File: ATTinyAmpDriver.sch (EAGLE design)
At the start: 28 parts, among them Q1 SI2301CDS, Q2 BC846, U1 SPX5205M5-L-3-3, U2 ATTINY5-TSHR, U3 MCP6L2-X_SN, X1 DIODES, X2 INPUT

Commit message: Working code and matching board and schematic
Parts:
- R3, R4: value 10k -> 3.9k
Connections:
- removed net INA+: C4.1, R4.2, U3.VINA+
- removed net VINB-: R8.1, R9.2, U3.VINB-
- new net INA-: R8.1, R9.2, U3.VINA-
- new net INB+: C4.1, R4.2, U3.VINB+
- net D-: now also U3.VINA+; no longer R3.1
- net MEASURE: now also C2.1, U3.VINB-; no longer R9.1
- net OUTA: now also R3.1, R9.1; no longer C2.1, U3.VINA-, U3.VINB+
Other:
- note added: "Q = .5 (ideal) f = 400Hz (~10% 3.77kHz PWM)"
- moved on the sheet: C4
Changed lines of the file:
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@@
 <attribute name="DIGIKEY_COST" value=".04"/>
 </part>
-<part name="R3" library="resistor" deviceset="R-US_" device="R0603" value="10k">
+<part name="R3" library="resistor" deviceset="R-US_" device="R0603" value="3.9k">
 <attribute name="DIGIKEY" value="RMCF0603FT10K0CT-ND"/>
 <attribute name="DIGIKEY_COST" value=".04"/>
@@
 <attribute name="DIGIKEY_COST" value=".64"/>
 </part>
-<part name="R4" library="resistor" deviceset="R-US_" device="R0603" value="10k">
+<part name="R4" library="resistor" deviceset="R-US_" device="R0603" value="3.9k">
 <attribute name="DIGIKEY" value="RMCF0603FT10K0CT-ND"/>
 <attribute name="DIGIKEY_COST" value=".04"/>
@@
 <wire x1="279.4" y1="215.9" x2="279.4" y2="0" width="0.1524" layer="98"/>
 <wire x1="279.4" y1="0" x2="0" y2="0" width="0.1524" layer="98"/>
-<text x="149.86" y="111.76" size="1.778" layer="91">Sallen Key PWM Input Filter</text>
+<text x="149.86" y="106.68" size="1.778" layer="91">Sallen Key PWM Input Filter</text>
+<text x="149.86" y="99.06" size="1.778" layer="91">Q = .5 (ideal)
+f = 400Hz (~10% 3.77kHz PWM)</text>
 </plain>
 <instances>
@@
 <attribute name="DIGIKEY_COST" x="165.1" y="124.46" size="1.778" layer="96" rot="MR180" display="off"/>
 </instance>
-<instance part="C4" gate="G$1" x="185.42" y="116.84">
-<attribute name="DIGIKEY" x="185.42" y="116.84" size="1.778" layer="96" display="off"/>
-<attribute name="DIGIKEY_COST" x="185.42" y="116.84" size="1.778" layer="96" display="off"/>
-</instance>
-<instance part="SUPPLY12" gate="GND" x="185.42" y="106.68"/>
+<instance part="C4" gate="G$1" x="190.5" y="116.84">
+<attribute name="DIGIKEY" x="190.5" y="116.84" size="1.778" layer="96" display="off"/>
+<attribute name="DIGIKEY_COST" x="190.5" y="116.84" size="1.778" layer="96" display="off"/>
+</instance>
+<instance part="SUPPLY12" gate="GND" x="190.5" y="106.68"/>
 <instance part="C6" gate="G$1" x="157.48" y="175.26">
 <attribute name="DIGIKEY" x="157.48" y="175.26" size="1.778" layer="96" display="off"/>
@@
 <pinref part="C4" gate="G$1" pin="2"/>
 <pinref part="SUPPLY12" gate="GND" pin="GND"/>
-<wire x1="185.42" y1="111.76" x2="185.42" y2="109.22" width="0.1524" layer="91"/>
-<wire x1="185.42" y1="109.22" x2="185.42" y2="106.68" width="0.1524" layer="91"/>
+<wire x1="190.5" y1="111.76" x2="190.5" y2="109.22" width="0.1524" layer="91"/>
+<wire x1="190.5" y1="109.22" x2="190.5" y2="106.68" width="0.1524" layer="91"/>
 </segment>
 <segment>
@@
 </segment>
 <segment>
-<pinref part="R3" gate="G$1" pin="1"/>
-<wire x1="160.02" y1="124.46" x2="157.48" y2="124.46" width="0.1524" layer="91"/>
-<label x="157.48" y="124.46" size="1.778" layer="95" rot="R180" xref="yes"/>
+<pinref part="U3" gate="A" pin="VINA+"/>
+<wire x1="193.04" y1="50.8" x2="190.5" y2="50.8" width="0.1524" layer="91"/>
+<label x="190.5" y="50.8" size="1.778" layer="95" rot="R180" xref="yes"/>
 </segment>
 </net>
@@
 </segment>
 <segment>
-<pinref part="R9" gate="G$1" pin="1"/>
-<wire x1="243.84" y1="132.08" x2="248.92" y2="132.08" width="0.1524" layer="91"/>
-<label x="248.92" y="132.08" size="1.778" layer="95" xref="yes"/>
-</segment>
-<segment>
 <pinref part="U3" gate="A" pin="VOUTB"/>
 <wire x1="233.68" y1="50.8" x2="241.3" y2="50.8" width="0.1524" layer="91"/>
 <label x="241.3" y="50.8" size="1.778" layer="95" xref="yes"/>
+</segment>
+<segment>
+<pinref part="C2" gate="G$1" pin="1"/>
+<wire x1="172.72" y1="137.16" x2="172.72" y2="142.24" width="0.1524" layer="91"/>
+<wire x1="172.72" y1="142.24" x2="162.56" y2="142.24" width="0.1524" layer="91"/>
+<label x="162.56" y="142.24" size="1.778" layer="95" rot="R180" xref="yes"/>
+</segment>
+<segment>
+<pinref part="U3" gate="A" pin="VINB-"/>
+<wire x1="193.04" y1="45.72" x2="182.88" y2="45.72" width="0.1524" layer="91"/>
+<label x="182.88" y="45.72" size="1.778" layer="95" rot="R180" xref="yes"/>
 </segment>
 </net>
@@
 </segment>
 </net>
-<net name="INA+" class="0">
-<segment>
-<pinref part="C4" gate="G$1" pin="1"/>
-<wire x1="185.42" y1="119.38" x2="185.42" y2="124.46" width="0.1524" layer="91"/>
-<pinref part="R4" gate="G$1" pin="2"/>
-<wire x1="185.42" y1="124.46" x2="193.04" y2="124.46" width="0.1524" layer="91"/>
-<label x="193.04" y="124.46" size="1.778" layer="95" xref="yes"/>
-</segment>
-<segment>
-<pinref part="U3" gate="A" pin="VINA+"/>
-<wire x1="193.04" y1="50.8" x2="180.34" y2="50.8" width="0.1524" layer="91"/>
-<label x="180.34" y="50.8" size="1.778" layer="95" rot="R180" xref="yes"/>
-</segment>
-</net>
 <net name="N$8" class="0">
 <segment>
@@
 </segment>
 <segment>
-<pinref part="U3" gate="A" pin="VINB+"/>
-<wire x1="193.04" y1="43.18" x2="180.34" y2="43.18" width="0.1524" layer="91"/>
-<label x="180.34" y="43.18" size="1.778" layer="95" rot="R180" xref="yes"/>
-</segment>
-<segment>
-<pinref part="C2" gate="G$1" pin="1"/>
-<wire x1="162.56" y1="142.24" x2="172.72" y2="142.24" width="0.1524" layer="91"/>
-<wire x1="172.72" y1="142.24" x2="172.72" y2="137.16" width="0.1524" layer="91"/>
-<label x="162.56" y="142.24" size="1.778" layer="95" rot="R180" xref="yes"/>
-</segment>
-<segment>
-<pinref part="U3" gate="A" pin="VINA-"/>
-<wire x1="193.04" y1="53.34" x2="190.5" y2="53.34" width="0.1524" layer="91"/>
-<label x="190.5" y="53.34" size="1.778" layer="95" rot="R180" xref="yes"/>
-</segment>
-</net>
-<net name="VINB-" class="0">
-<segment>
-<pinref part="U3" gate="A" pin="VINB-"/>
-<wire x1="193.04" y1="45.72" x2="190.5" y2="45.72" width="0.1524" layer="91"/>
-<label x="190.5" y="45.72" size="1.778" layer="95" rot="R180" xref="yes"/>
-</segment>
-<segment>
-<wire x1="220.98" y1="132.08" x2="228.6" y2="132.08" width="0.1524" layer="91"/>
-<pinref part="R9" gate="G$1" pin="2"/>
-<wire x1="228.6" y1="132.08" x2="228.6" y2="129.54" width="0.1524" layer="91"/>
-<wire x1="233.68" y1="132.08" x2="228.6" y2="132.08" width="0.1524" layer="91"/>
-<junction x="228.6" y="132.08"/>
-<label x="220.98" y="132.08" size="1.778" layer="95" rot="R180" xref="yes"/>
-<pinref part="R8" gate="G$1" pin="1"/>
+<pinref part="R9" gate="G$1" pin="1"/>
+<wire x1="243.84" y1="132.08" x2="251.46" y2="132.08" width="0.1524" layer="91"/>
+<label x="251.46" y="132.08" size="1.778" layer="95" xref="yes"/>
+</segment>
+<segment>
+<pinref part="R3" gate="G$1" pin="1"/>
+<wire x1="160.02" y1="124.46" x2="154.94" y2="124.46" width="0.1524" layer="91"/>
+<label x="154.94" y="124.46" size="1.778" layer="95" rot="R180" xref="yes"/>
 </segment>
 </net>
@@
 </segment>
 </net>
+<net name="INB+" class="0">
+<segment>
+<pinref part="R4" gate="G$1" pin="2"/>
+<pinref part="C4" gate="G$1" pin="1"/>
+<wire x1="185.42" y1="124.46" x2="190.5" y2="124.46" width="0.1524" layer="91"/>
+<wire x1="190.5" y1="124.46" x2="190.5" y2="119.38" width="0.1524" layer="91"/>
+<wire x1="190.5" y1="124.46" x2="195.58" y2="124.46" width="0.1524" layer="91"/>
+<junction x="190.5" y="124.46"/>
+<label x="195.58" y="124.46" size="1.778" layer="95" xref="yes"/>
+</segment>
+<segment>
+<pinref part="U3" gate="A" pin="VINB+"/>
+<wire x1="193.04" y1="43.18" x2="190.5" y2="43.18" width="0.1524" layer="91"/>
+<label x="190.5" y="43.18" size="1.778" layer="95" rot="R180" xref="yes"/>
+</segment>
+</net>
+<net name="INA-" class="0">
+<segment>
+<pinref part="U3" gate="A" pin="VINA-"/>
+<wire x1="193.04" y1="53.34" x2="182.88" y2="53.34" width="0.1524" layer="91"/>
+<label x="182.88" y="53.34" size="1.778" layer="95" rot="R180" xref="yes"/>
+</segment>
+<segment>
+<pinref part="R9" gate="G$1" pin="2"/>
+<wire x1="233.68" y1="132.08" x2="228.6" y2="132.08" width="0.1524" layer="91"/>
+<pinref part="R8" gate="G$1" pin="1"/>
+<wire x1="228.6" y1="132.08" x2="218.44" y2="132.08" width="0.1524" layer="91"/>
+<wire x1="228.6" y1="129.54" x2="228.6" y2="132.08" width="0.1524" layer="91"/>
+<junction x="228.6" y="132.08"/>
+<label x="218.44" y="132.08" size="1.778" layer="95" rot="R180" xref="yes"/>
+</segment>
+</net>

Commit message: Updated BOM
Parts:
- R3, R4: DIGIKEY RMCF0603FT10K0CT-ND -> RMCF0603FT3K90CT-ND
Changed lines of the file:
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@@
 </part>
 <part name="R3" library="resistor" deviceset="R-US_" device="R0603" value="3.9k">
-<attribute name="DIGIKEY" value="RMCF0603FT10K0CT-ND"/>
+<attribute name="DIGIKEY" value="RMCF0603FT3K90CT-ND"/>
 <attribute name="DIGIKEY_COST" value=".04"/>
 </part>
@@
 </part>
 <part name="R4" library="resistor" deviceset="R-US_" device="R0603" value="3.9k">
-<attribute name="DIGIKEY" value="RMCF0603FT10K0CT-ND"/>
+<attribute name="DIGIKEY" value="RMCF0603FT3K90CT-ND"/>
 <attribute name="DIGIKEY_COST" value=".04"/>
 </part>

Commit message: Added Newark pricing to some components
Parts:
- Q1: NEWARK (none) -> 16P3701; NEWARK_COST (none) -> .37
- Q2: NEWARK (none) -> 75R0728; NEWARK_COST (none) -> .14
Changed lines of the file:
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@@
 <attribute name="DIGIKEY" value="568-6956-1-ND"/>
 <attribute name="DIGIKEY_COST" value=".69"/>
+<attribute name="NEWARK" value="16P3701"/>
+<attribute name="NEWARK_COST" value=".37"/>
 </part>
 <part name="SUPPLY11" library="supply2" deviceset="+14V" device=""/>
@@
 <attribute name="DIGIKEY" value="BC846BMTFCT-ND"/>
 <attribute name="DIGIKEY_COST" value=".17"/>
+<attribute name="NEWARK" value="75R0728"/>
+<attribute name="NEWARK_COST" value=".14"/>
 </part>
 <part name="SUPPLY14" library="supply2" deviceset="GND" device=""/>
@@
 <attribute name="VALUE" x="90.17" y="66.04" size="1.778" layer="96" rot="MR180"/>
 <attribute name="NAME" x="92.71" y="76.2" size="1.778" layer="95" rot="MR180"/>
+<attribute name="NEWARK" x="96.52" y="71.12" size="1.778" layer="96" rot="MR180" display="off"/>
+<attribute name="NEWARK_COST" x="96.52" y="71.12" size="1.778" layer="96" rot="MR180" display="off"/>
 </instance>
 <instance part="SUPPLY11" gate="G$1" x="101.6" y="93.98"/>
@@
 <attribute name="DIGIKEY" x="76.2" y="60.96" size="1.778" layer="96" display="off"/>
 <attribute name="DIGIKEY_COST" x="76.2" y="60.96" size="1.778" layer="96" display="off"/>
+<attribute name="NEWARK" x="76.2" y="60.96" size="1.778" layer="96" display="off"/>
+<attribute name="NEWARK_COST" x="76.2" y="60.96" size="1.778" layer="96" display="off"/>
 </instance>
 <instance part="SUPPLY14" gate="GND" x="78.74" y="50.8"/>

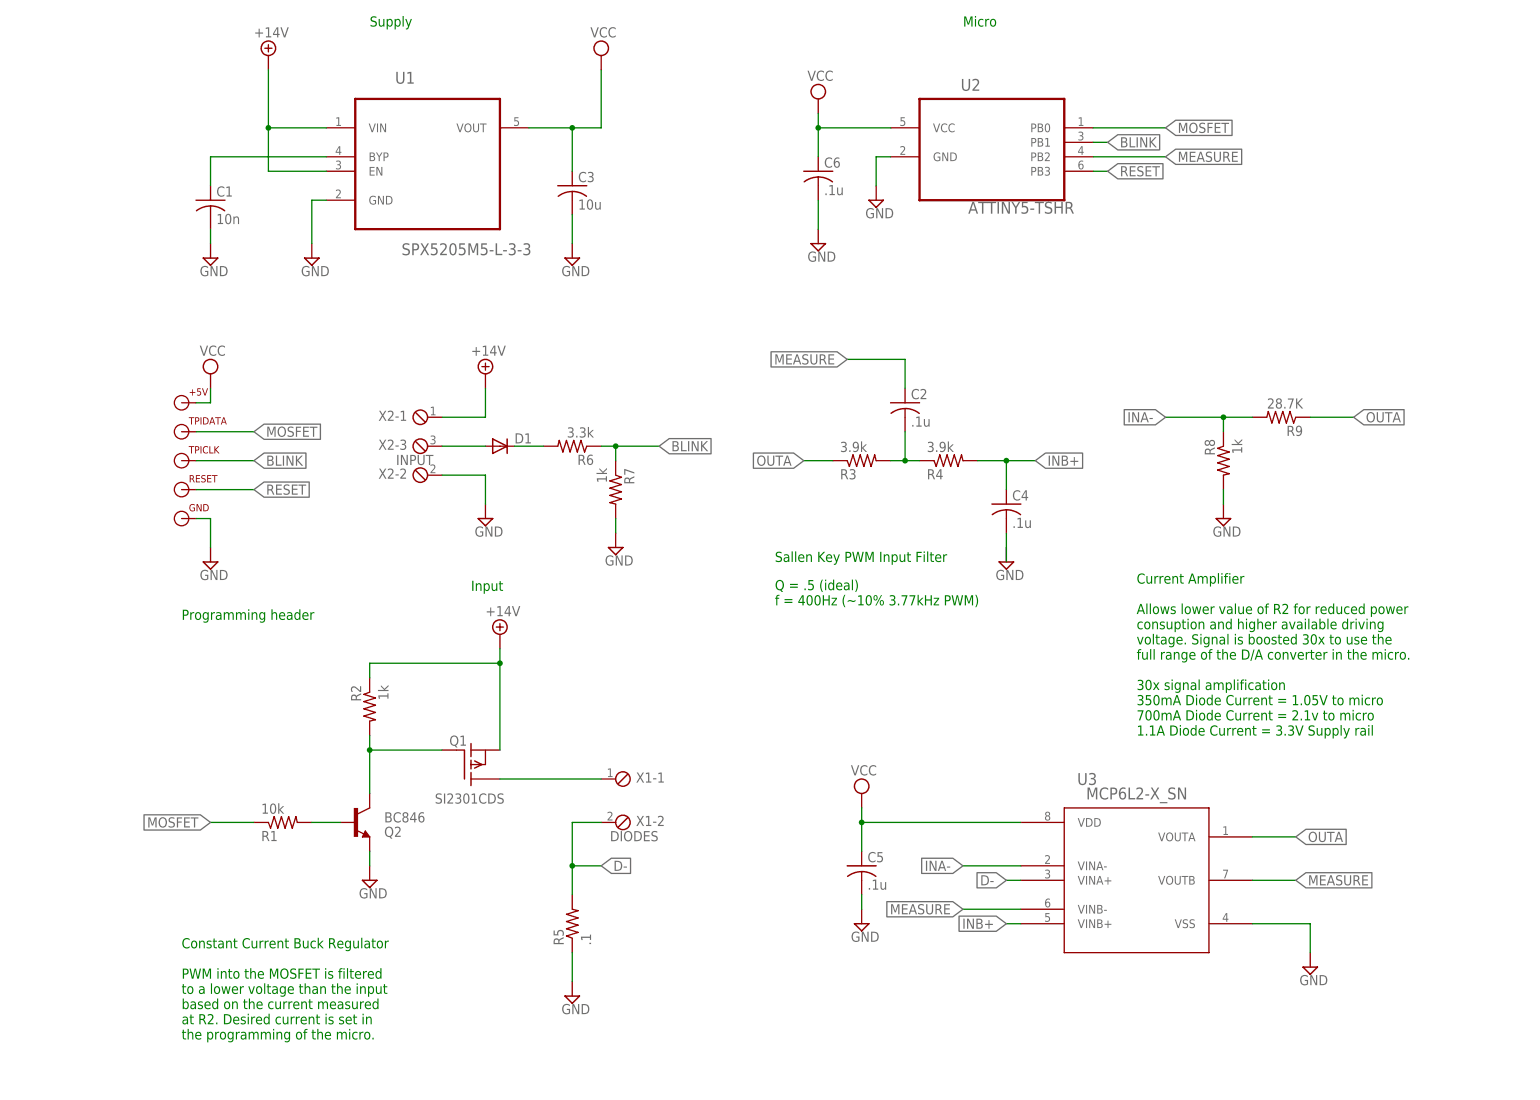
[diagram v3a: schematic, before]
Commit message: Added test points around op-amp filter
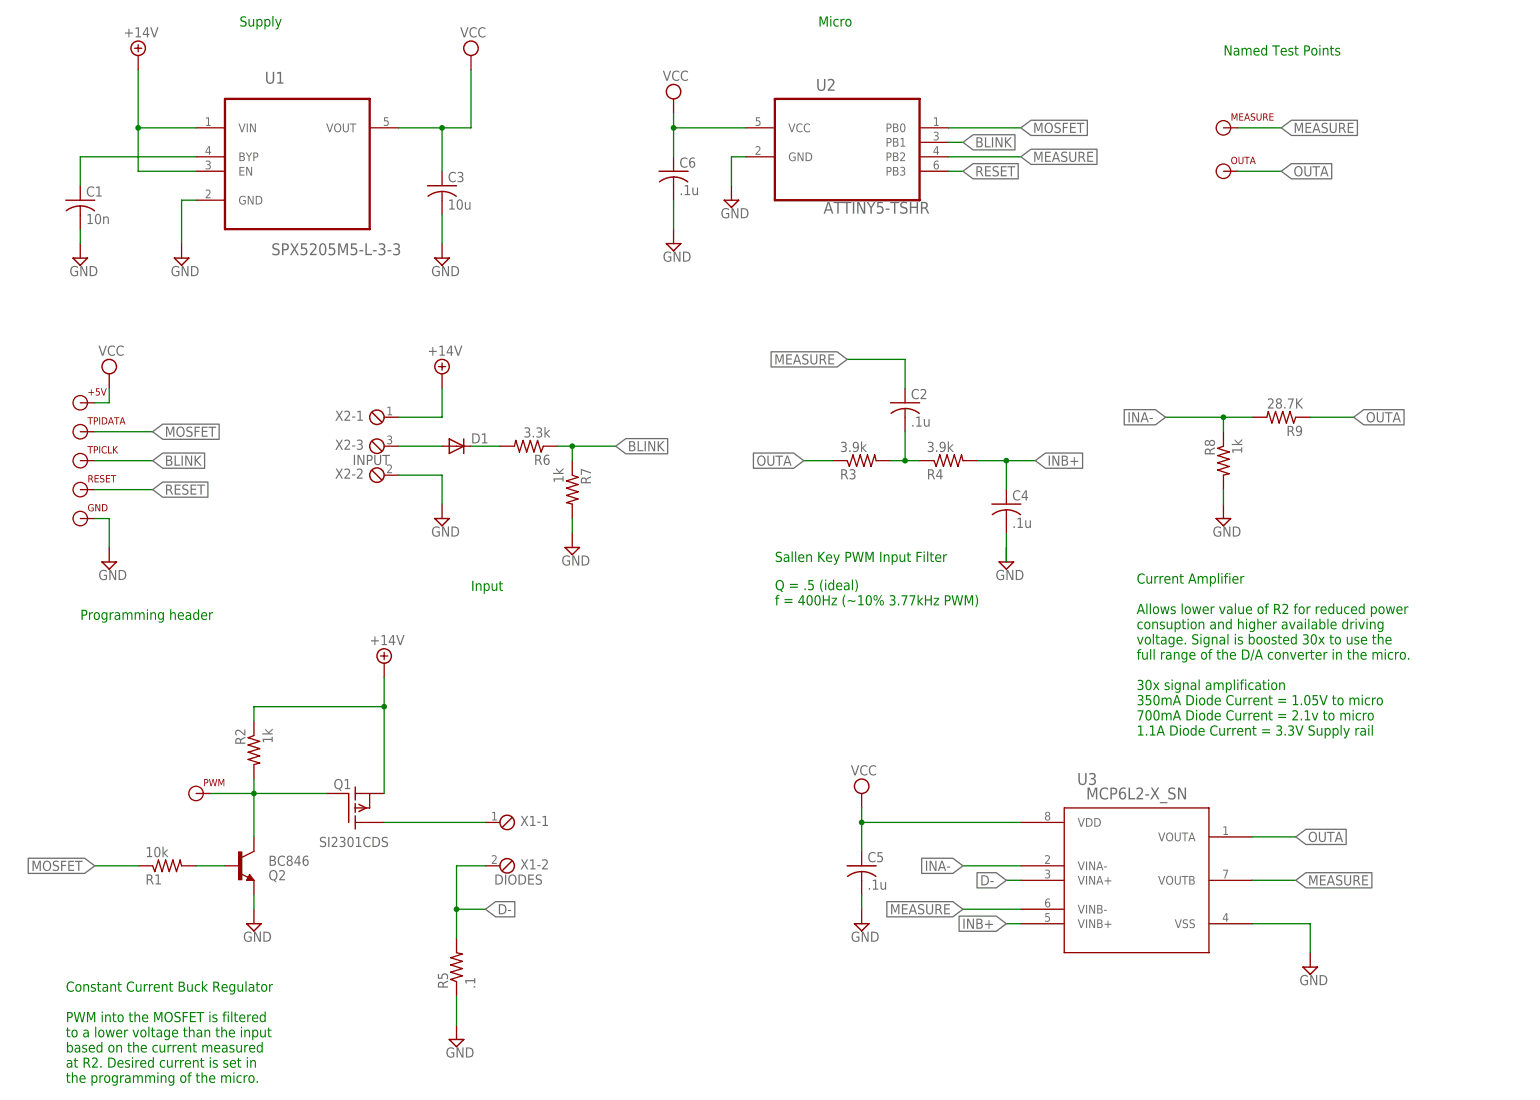
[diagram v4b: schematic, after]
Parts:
- added MEASURE, OUTA, PWM: TPI, Personal:TPI
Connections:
- net MEASURE: now also MEASURE.TPI_PIN
- net N$5: now also PWM.TPI_PIN
- net OUTA: now also OUTA.TPI_PIN
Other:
- note added: "Named Test Points"
- moved on the sheet: +5V, C1, C3, C6, D1, GND, Q1, Q2, R1, R2, R5, R6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

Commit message: Changed C3 to 1206 47uF
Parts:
- C3: value 10u -> 47u; device resistor:C-USC0805 -> resistor:C-USC1206; DIGIKEY 445-7534-1-ND -> 399-5508-1-ND; DIGIKEY_COST .10 -> .67
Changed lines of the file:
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@@
 <part name="SUPPLY2" library="supply2" deviceset="GND" device=""/>
 <part name="SUPPLY3" library="supply2" deviceset="VCC" device=""/>
-<part name="C3" library="resistor" deviceset="C-US" device="C0805" value="10u">
-<attribute name="DIGIKEY" value="445-7534-1-ND"/>
-<attribute name="DIGIKEY_COST" value=".10"/>
+<part name="C3" library="resistor" deviceset="C-US" device="C1206" value="47u">
+<attribute name="DIGIKEY" value="399-5508-1-ND"/>
+<attribute name="DIGIKEY_COST" value=".67"/>
 </part>
 <part name="SUPPLY4" library="supply2" deviceset="GND" device=""/>

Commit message: Created Programming Fixture
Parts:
- +5V, GND, MEASURE, OUTA, PWM, RESET, TPICLK, TPIDATA: device Personal:TPI -> Combined:TPI
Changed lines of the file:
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@@
 <layer number="97" name="Info" color="7" fill="1" visible="yes" active="yes"/>
 <layer number="98" name="Guide" color="6" fill="1" visible="yes" active="yes"/>
+<layer number="100" name="TestPads" color="7" fill="1" visible="yes" active="yes"/>
 <layer number="250" name="Descript" color="3" fill="1" visible="no" active="no"/>
 <layer number="251" name="SMDround" color="12" fill="11" visible="no" active="no"/>
@@
 <attribute name="DIGIKEY_COST" value=".04"/>
 </part>
-<part name="TPIDATA" library="Personal" deviceset="TPI" device=""/>
-<part name="TPICLK" library="Personal" deviceset="TPI" device=""/>
-<part name="+5V" library="Personal" deviceset="TPI" device=""/>
-<part name="GND" library="Personal" deviceset="TPI" device=""/>
+<part name="TPIDATA" library="Combined" deviceset="TPI" device=""/>
+<part name="TPICLK" library="Combined" deviceset="TPI" device=""/>
+<part name="+5V" library="Combined" deviceset="TPI" device=""/>
+<part name="GND" library="Combined" deviceset="TPI" device=""/>
 <part name="SUPPLY15" library="supply2" deviceset="VCC" device=""/>
 <part name="SUPPLY16" library="supply2" deviceset="GND" device=""/>
@@
 </part>
 <part name="SUPPLY17" library="supply2" deviceset="GND" device=""/>
-<part name="RESET" library="Personal" deviceset="TPI" device=""/>
+<part name="RESET" library="Combined" deviceset="TPI" device=""/>
 <part name="SUPPLY19" library="supply2" deviceset="GND" device=""/>
 <part name="SUPPLY21" library="supply2" deviceset="VCC" device=""/>
@@
 <attribute name="DIGIKEY_COST" value=".04"/>
 </part>
-<part name="PWM" library="Personal" deviceset="TPI" device=""/>
-<part name="MEASURE" library="Personal" deviceset="TPI" device=""/>
-<part name="OUTA" library="Personal" deviceset="TPI" device=""/>
+<part name="PWM" library="Combined" deviceset="TPI" device=""/>
+<part name="MEASURE" library="Combined" deviceset="TPI" device=""/>
+<part name="OUTA" library="Combined" deviceset="TPI" device=""/>
 </parts>
 <sheets>
